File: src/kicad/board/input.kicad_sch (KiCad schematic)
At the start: 21 parts

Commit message: update pcb
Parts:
- C10, C11: renamed from C?; footprint (none) -> Capacitor_SMD:C_0805_2012Metric
- R14, R15, R16, R17, R18, R19, R20, R21, R22, R23: renamed from R?; footprint (none) -> Resistor_SMD:R_0805_2012Metric
- SW1, SW2, SW4, SW5: renamed from SW?; footprint (none) -> Button_Switch_Keyboard:SW_Cherry_MX_1.00u_PCB
- SW3: renamed from SW?; footprint (none) -> Rotary_Encoder:RotaryEncoder_Bourns_Vertical_PEC12R-3xxxF-Sxxxx
- U5: renamed from U?; footprint (none) -> Library:74HC4051
- gave numbers to parts that had none: 1
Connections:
- net +5V renamed VDD

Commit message: update wip
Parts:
- R14, R15, R16: value 10K -> 2K7
- U6: footprint (none) -> Library:CD4072BM96
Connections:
- net VDD renamed +3.3V

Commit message: update
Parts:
- C10, C11: Vendor (none) -> C28233
- R14, R15, R16: Vendor (none) -> C17530
- R17, R18, R19, R20, R21, R22, R23: Vendor (none) -> C17414
- U5: footprint Library:74HC4051 -> Package_SO:SOIC-16_3.9x9.9mm_P1.27mm; Vendor (none) -> C507180
- U6: footprint Library:CD4072BM96 -> Package_SO:SOIC-14_3.9x8.7mm_P1.27mm; Vendor (none) -> C2862967
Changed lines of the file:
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@@
   (junction (at 135.89 76.2) (diameter 0) (color 0 0 0 0)
   )
-  (junction (at 82.55 102.87) (diameter 0) (color 0 0 0 0)
+  (junction (at 82.55 106.68) (diameter 0) (color 0 0 0 0)
   )
   (junction (at 185.42 113.03) (diameter 0) (color 0 0 0 0)
   )
-  (junction (at 93.98 102.87) (diameter 0) (color 0 0 0 0)
+  (junction (at 93.98 106.68) (diameter 0) (color 0 0 0 0)
   )
   (junction (at 74.93 83.82) (diameter 0) (color 0 0 0 0)
@@
   (junction (at 135.89 50.8) (diameter 0) (color 0 0 0 0)
   )
-  (junction (at 86.36 102.87) (diameter 0) (color 0 0 0 0)
+  (junction (at 86.36 106.68) (diameter 0) (color 0 0 0 0)
   )
   (junction (at 78.74 86.36) (diameter 0) (color 0 0 0 0)
@@
   (junction (at 185.42 124.46) (diameter 0) (color 0 0 0 0)
   )
-  (junction (at 78.74 102.87) (diameter 0) (color 0 0 0 0)
+  (junction (at 78.74 106.68) (diameter 0) (color 0 0 0 0)
   )
   (junction (at 203.2 113.03) (diameter 0) (color 0 0 0 0)
@@
     (stroke (width 0) (type default) (color 0 0 0 0))
   )
-  (wire (pts (xy 78.74 102.87) (xy 82.55 102.87))
+  (wire (pts (xy 78.74 106.68) (xy 82.55 106.68))
     (stroke (width 0) (type default) (color 0 0 0 0))
   )
@@
     (stroke (width 0) (type default) (color 0 0 0 0))
   )
-  (wire (pts (xy 78.74 99.06) (xy 78.74 102.87))
+  (wire (pts (xy 78.74 99.06) (xy 78.74 106.68))
     (stroke (width 0) (type default) (color 0 0 0 0))
   )
@@
     (stroke (width 0) (type default) (color 0 0 0 0))
   )
-  (wire (pts (xy 82.55 99.06) (xy 82.55 102.87))
+  (wire (pts (xy 82.55 99.06) (xy 82.55 106.68))
     (stroke (width 0) (type default) (color 0 0 0 0))
   )
@@
     (stroke (width 0) (type default) (color 0 0 0 0))
   )
-  (wire (pts (xy 78.74 102.87) (xy 78.74 104.14))
+  (wire (pts (xy 78.74 106.68) (xy 78.74 107.95))
     (stroke (width 0) (type default) (color 0 0 0 0))
   )
@@
     (stroke (width 0) (type default) (color 0 0 0 0))
   )
-  (wire (pts (xy 74.93 99.06) (xy 74.93 102.87))
+  (wire (pts (xy 74.93 99.06) (xy 74.93 106.68))
     (stroke (width 0) (type default) (color 0 0 0 0))
   )
@@
     (stroke (width 0) (type default) (color 0 0 0 0))
   )
-  (wire (pts (xy 86.36 93.98) (xy 86.36 102.87))
+  (wire (pts (xy 86.36 93.98) (xy 86.36 106.68))
     (stroke (width 0) (type default) (color 0 0 0 0))
   )
@@
     (stroke (width 0) (type default) (color 0 0 0 0))
   )
-  (wire (pts (xy 93.98 102.87) (xy 93.98 101.6))
+  (wire (pts (xy 93.98 101.6) (xy 93.98 106.68))
     (stroke (width 0) (type default) (color 0 0 0 0))
   )
@@
     (stroke (width 0) (type default) (color 0 0 0 0))
   )
-  (wire (pts (xy 74.93 102.87) (xy 78.74 102.87))
+  (wire (pts (xy 74.93 106.68) (xy 78.74 106.68))
     (stroke (width 0) (type default) (color 0 0 0 0))
   )
@@
     (stroke (width 0) (type default) (color 0 0 0 0))
   )
-  (wire (pts (xy 96.52 102.87) (xy 96.52 101.6))
+  (wire (pts (xy 96.52 101.6) (xy 96.52 106.68))
     (stroke (width 0) (type default) (color 0 0 0 0))
   )
@@
     (stroke (width 0) (type default) (color 0 0 0 0))
   )
-  (wire (pts (xy 93.98 102.87) (xy 96.52 102.87))
+  (wire (pts (xy 93.98 106.68) (xy 96.52 106.68))
     (stroke (width 0) (type default) (color 0 0 0 0))
   )
@@
     (stroke (width 0) (type default) (color 0 0 0 0))
   )
-  (wire (pts (xy 86.36 102.87) (xy 93.98 102.87))
+  (wire (pts (xy 86.36 106.68) (xy 93.98 106.68))
     (stroke (width 0) (type default) (color 0 0 0 0))
   )
@@
     (stroke (width 0) (type default) (color 0 0 0 0))
   )
-  (wire (pts (xy 86.36 102.87) (xy 82.55 102.87))
+  (wire (pts (xy 86.36 106.68) (xy 82.55 106.68))
     (stroke (width 0) (type default) (color 0 0 0 0))
   )
@@
       (effects (font (size 1.27 1.27)) hide)
     )
+    (property "Vendor" "C17414" (id 4) (at 177.8 54.61 0)
+      (effects (font (size 1.27 1.27)) hide)
+    )
     (pin "1")
     (pin "2")
@@
       (effects (font (size 1.27 1.27)) (justify left))
     )
-    (property "Footprint" "Library:74HC4051" (id 2) (at 93.98 96.52 0)
+    (property "Footprint" "Package_SO:SOIC-16_3.9x9.9mm_P1.27mm" (id 2) (at 93.98 96.52 0)
       (effects (font (size 1.27 1.27)) hide)
     )
     (property "Datasheet" "http://www.ti.com/lit/ds/symlink/cd74hc4051.pdf" (id 3) (at 93.98 96.52 0)
+      (effects (font (size 1.27 1.27)) hide)
+    )
+    (property "Vendor" "C507180" (id 4) (at 93.98 86.36 0)
       (effects (font (size 1.27 1.27)) hide)
     )
@@
       (effects (font (size 1.27 1.27)) hide)
     )
+    (property "Vendor" "C17530" (id 4) (at 82.55 95.25 0)
+      (effects (font (size 1.27 1.27)) hide)
+    )
     (pin "1")
     (pin "2")
@@
       (effects (font (size 1.27 1.27)) hide)
     )
+    (property "Vendor" "C17414" (id 4) (at 204.47 54.61 0)
+      (effects (font (size 1.27 1.27)) hide)
+    )
     (pin "1")
     (pin "2")
@@
     )
     (property "Datasheet" "~" (id 3) (at 78.74 95.25 0)
+      (effects (font (size 1.27 1.27)) hide)
+    )
+    (property "Vendor" "C17530" (id 4) (at 78.74 95.25 0)
       (effects (font (size 1.27 1.27)) hide)
     )
@@
       (effects (font (size 1.27 1.27)) hide)
     )
+    (property "Vendor" "C28233" (id 4) (at 124.46 63.5 0)
+      (effects (font (size 1.27 1.27)) hide)
+    )
     (pin "1")
     (pin "2")
@@
       (effects (font (size 1.27 1.27)) hide)
     )
+    (property "Vendor" "C28233" (id 4) (at 82.55 66.04 0)
+      (effects (font (size 1.27 1.27)) hide)
+    )
     (pin "1")
     (pin "2")
@@
     )
     (property "Datasheet" "~" (id 3) (at 181.61 118.11 0)
+      (effects (font (size 1.27 1.27)) hide)
+    )
+    (property "Vendor" "C17414" (id 4) (at 181.61 118.11 0)
       (effects (font (size 1.27 1.27)) hide)
     )
@@
     (property "Reference" "U6" (id 0) (at 138.43 110.49 0))
     (property "Value" "4072" (id 1) (at 138.43 113.03 0))
-    (property "Footprint" "Library:CD4072BM96" (id 2) (at 138.43 111.76 0)
+    (property "Footprint" "Package_SO:SOIC-14_3.9x8.7mm_P1.27mm" (id 2) (at 138.43 111.76 0)
       (effects (font (size 1.27 1.27)) hide)
     )
     (property "Datasheet" "http://www.intersil.com/content/dam/Intersil/documents/cd40/cd4071bms-72bms-75bms.pdf" (id 3) (at 138.43 111.76 0)
+      (effects (font (size 1.27 1.27)) hide)
+    )
+    (property "Vendor" "C2862967" (id 4) (at 138.43 111.76 0)
       (effects (font (size 1.27 1.27)) hide)
     )
@@
       (effects (font (size 1.27 1.27)) hide)
     )
+    (property "Vendor" "C17414" (id 4) (at 185.42 118.11 0)
+      (effects (font (size 1.27 1.27)) hide)
+    )
     (pin "1")
     (pin "2")
@@
       (effects (font (size 1.27 1.27)) (justify left))
     )
-    (property "Footprint" "Library:CD4072BM96" (id 2) (at 135.89 63.5 0)
+    (property "Footprint" "Package_SO:SOIC-14_3.9x8.7mm_P1.27mm" (id 2) (at 135.89 63.5 0)
       (effects (font (size 1.27 1.27)) hide)
     )
     (property "Datasheet" "http://www.intersil.com/content/dam/Intersil/documents/cd40/cd4071bms-72bms-75bms.pdf" (id 3) (at 135.89 63.5 0)
+      (effects (font (size 1.27 1.27)) hide)
+    )
+    (property "Vendor" "C2862967" (id 4) (at 135.89 63.5 0)
       (effects (font (size 1.27 1.27)) hide)
     )
@@
       (effects (font (size 1.27 1.27)) hide)
     )
+    (property "Vendor" "C17414" (id 4) (at 204.47 78.74 0)
+      (effects (font (size 1.27 1.27)) hide)
+    )
     (pin "1")
     (pin "2")
@@
       (effects (font (size 1.27 1.27)) hide)
     )
+    (property "Vendor" "C17530" (id 4) (at 74.93 95.25 0)
+      (effects (font (size 1.27 1.27)) hide)
+    )
     (pin "1")
     (pin "2")
@@
     (pin "1")
   )
-  (symbol (lib_id "power:GND") (at 78.74 104.14 0) (unit 1)
-    (in_bom yes) (on_board yes) (fields_autoplaced)
-    (property "Reference" "#PWR0117" (id 0) (at 78.74 110.49 0)
-      (effects (font (size 1.27 1.27)) hide)
-    )
-    (property "Value" "GND" (id 1) (at 78.74 109.22 0))
-    (property "Footprint" "" (id 2) (at 78.74 104.14 0)
-      (effects (font (size 1.27 1.27)) hide)
-    )
-    (property "Datasheet" "" (id 3) (at 78.74 104.14 0)
+  (symbol (lib_id "power:GND") (at 78.74 107.95 0) (unit 1)
+    (in_bom yes) (on_board yes) (fields_autoplaced)
+    (property "Reference" "#PWR0117" (id 0) (at 78.74 114.3 0)
+      (effects (font (size 1.27 1.27)) hide)
+    )
+    (property "Value" "GND" (id 1) (at 78.74 113.03 0))
+    (property "Footprint" "" (id 2) (at 78.74 107.95 0)
+      (effects (font (size 1.27 1.27)) hide)
+    )
+    (property "Datasheet" "" (id 3) (at 78.74 107.95 0)
       (effects (font (size 1.27 1.27)) hide)
     )
@@
     )
     (property "Datasheet" "~" (id 3) (at 177.8 78.74 0)
+      (effects (font (size 1.27 1.27)) hide)
+    )
+    (property "Vendor" "C17414" (id 4) (at 177.8 78.74 0)
       (effects (font (size 1.27 1.27)) hide)
     )
@@
     (property "Reference" "U6" (id 0) (at 138.43 97.79 0))
     (property "Value" "4072" (id 1) (at 138.43 100.33 0))
-    (property "Footprint" "Library:CD4072BM96" (id 2) (at 138.43 99.06 0)
+    (property "Footprint" "Package_SO:SOIC-14_3.9x8.7mm_P1.27mm" (id 2) (at 138.43 99.06 0)
       (effects (font (size 1.27 1.27)) hide)
     )
     (property "Datasheet" "http://www.intersil.com/content/dam/Intersil/documents/cd40/cd4071bms-72bms-75bms.pdf" (id 3) (at 138.43 99.06 0)
+      (effects (font (size 1.27 1.27)) hide)
+    )
+    (property "Vendor" "C2862967" (id 4) (at 138.43 99.06 0)
       (effects (font (size 1.27 1.27)) hide)
     )
@@
       (effects (font (size 1.27 1.27)) hide)
     )
+    (property "Vendor" "C17414" (id 4) (at 203.2 118.11 0)
+      (effects (font (size 1.27 1.27)) hide)
+    )

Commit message: update
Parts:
- renumbered C10 to C3, C11 to C4, R17 to R10, R18 to R11, R19 to R12, R20 to R13, R21 to R14, R22 to R15, R23 to R16, R14 to R7, R15 to R8, R16 to R9, U5 to U2, U6 to U3
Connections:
- net +3.3V renamed 3.3V_LOCAL
- net GND renamed GND_LOCAL
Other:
- moved on the sheet: C3, C4, R10, R11, R12, R13, R14, R15, R16, R7, R8, R9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

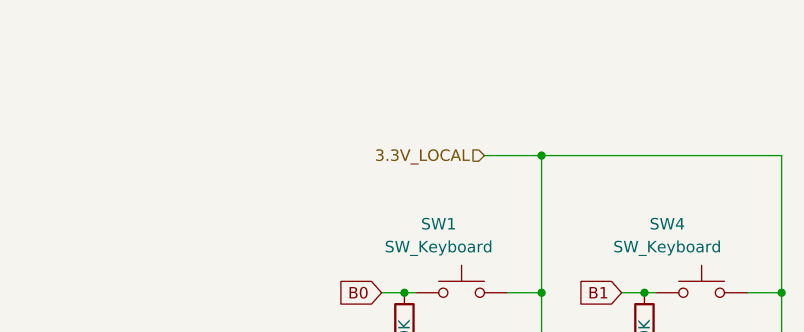
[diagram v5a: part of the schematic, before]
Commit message: working with current hardware. still a race condition somewhere with muting i think
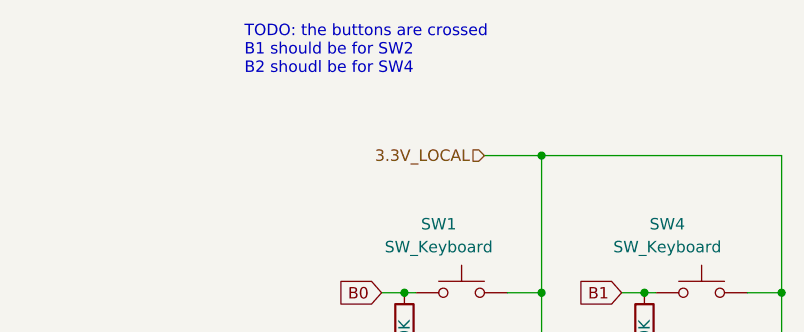
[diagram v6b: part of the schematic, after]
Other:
- note added: "TODO: the buttons are crossed B1 should be for SW2 B2 shoudl be for SW4"
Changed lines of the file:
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@@
     (stroke (width 0) (type default) (color 0 0 0 0))
+  )
+  (text "TODO: the buttons are crossed\nB1 should be for SW2\nB2 shoudl be for SW4"
+    (at 184.15 34.29 0)
+    (effects (font (size 1.27 1.27)) (justify left bottom))
   )
   (text "todo: make local?\n" (at 133.985 134.62 0)

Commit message: update
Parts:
- removed C3, C4: 0.1uF, Capacitor_SMD:C_0805_2012Metric, symbol Device:C
- removed R10, R11, R12, R13, R14, R15, R16: 10K, Resistor_SMD:R_0805_2012Metric, symbol Device:R
- removed R7, R8, R9: 2K7, Resistor_SMD:R_0805_2012Metric, symbol Device:R
- removed U2: 74HC4051, Package_SO:SOIC-16_3.9x9.9mm_P1.27mm, symbol 74xx:74HC4051
- removed U3: 4072, Package_SO:SOIC-14_3.9x8.7mm_P1.27mm, symbol 4xxx:4072
- added C?: 0.1uF, Capacitor_SMD:C_0805_2012Metric, symbol Device:C
- added U?: MCP23017_ML, Package_DFN_QFN:QFN-28-1EP_6x6mm_P0.65mm_EP4.25x4.25mm, symbol Interface_Expansion:MCP23017_ML
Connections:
- net 3.3V_LOCAL: now also C?.1, U?.14 (~{RESET}), U?.5 (VDD); no longer SW1.2, SW2.2, SW3.C, SW3.S1, SW4.2, SW5.2
- net B0: now also U?.25 (GPB0)
- net B1: now also SW2.1, U?.26 (GPB1); no longer SW4.1
- net B2: now also SW4.1, U?.27 (GPB2); no longer SW2.1
- net B3: now also U?.28 (GPB3)
- net B4: now also U?.1 (GPB4)
- net B5: now also U?.2 (GPB5)
- net B6: now also U?.3 (GPB6)
- net GND_LOCAL: now also SW1.2, SW2.2, SW3.C, SW3.S1, SW4.2, SW5.2, C?.2, U?.11 (A0), U?.12 (A1), U?.13 (A2), U?.29 (EP), U?.6 (VSS)
- new net INT: U?.15 (INTB)
- new net SCK: U?.8 (SCK)
- new net SDA: U?.9 (SDA)
- no-connect marks 0 -> 10
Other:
- note removed: "TODO: the buttons are crossed B1 should be for SW2 B2 shoudl be for SW4"
- note removed: "todo: make local?"
- moved on the sheet: SW1, SW2, SW3, SW4, SW5

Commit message: update
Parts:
- U?: Vendor (none) -> C629439
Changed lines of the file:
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@@
       (effects (font (size 1.27 1.27)) (justify left) hide)
+    )
+    (property "Vendor" "C629439" (id 4) (at 118.11 96.52 0)
+      (effects (font (size 1.27 1.27)) hide)
     )
     (pin "1")
